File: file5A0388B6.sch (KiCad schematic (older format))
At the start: 40 parts, among them J1 test, J2 test, J3 test, J4 test, U1 AD7175-8, U2 ADR4520, U3 ADR445, Y1 16M

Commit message: 전해콘덴서 foot print 변경
전해 콘덴서 변경
Bypass 콘데서 OPAMP에 추가 하여야 함
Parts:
- C1, C10, C12, C18, C19, C2, C7: footprint Capacitors_SMD:C_1812_HandSoldering -> USER:C_1812_HandSoldering_Polar
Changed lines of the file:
@@
 F 0 "C2" H 3475 2350 50  0000 L CNN
 F 1 "10uF" H 3475 2150 50  0000 L CNN
-F 2 "Capacitors_SMD:C_1812_HandSoldering" H 3450 2250 50  0001 C CNN
+F 2 "USER:C_1812_HandSoldering_Polar" H 3450 2250 50  0001 C CNN
 F 3 "" H 3450 2250 50  0001 C CNN
 	1    3450 2250
@@
 F 0 "C1" H 3475 1400 50  0000 L CNN
 F 1 "10uF" H 3475 1200 50  0000 L CNN
-F 2 "Capacitors_SMD:C_1812_HandSoldering" H 3450 1300 50  0001 C CNN
+F 2 "USER:C_1812_HandSoldering_Polar" H 3450 1300 50  0001 C CNN
 F 3 "" H 3450 1300 50  0001 C CNN
 	1    3450 1300
@@
 F 0 "C12" H 6375 2250 50  0000 L CNN
 F 1 "10uF" H 6375 2050 50  0000 L CNN
-F 2 "Capacitors_SMD:C_1812_HandSoldering" H 6350 2150 50  0001 C CNN
+F 2 "USER:C_1812_HandSoldering_Polar" H 6350 2150 50  0001 C CNN
 F 3 "" H 6350 2150 50  0001 C CNN
 	1    6350 2150
@@
 F 0 "C10" H 5725 2500 50  0000 L CNN
 F 1 "10uF" H 5725 2300 50  0000 L CNN
-F 2 "Capacitors_SMD:C_1812_HandSoldering" H 5700 2400 50  0001 C CNN
+F 2 "USER:C_1812_HandSoldering_Polar" H 5700 2400 50  0001 C CNN
 F 3 "" H 5700 2400 50  0001 C CNN
 	1    5700 2400
@@
 F 0 "C7" H 5325 1400 50  0000 L CNN
 F 1 "10uF" H 5325 1200 50  0000 L CNN
-F 2 "Capacitors_SMD:C_1812_HandSoldering" H 5300 1300 50  0001 C CNN
+F 2 "USER:C_1812_HandSoldering_Polar" H 5300 1300 50  0001 C CNN
 F 3 "" H 5300 1300 50  0001 C CNN
 	1    5300 1300
@@
 F 0 "C19" H 9275 5300 50  0000 L CNN
 F 1 "10uF" H 9275 5100 50  0000 L CNN
-F 2 "Capacitors_SMD:C_1812_HandSoldering" H 9250 5200 50  0001 C CNN
+F 2 "USER:C_1812_HandSoldering_Polar" H 9250 5200 50  0001 C CNN
 F 3 "" H 9250 5200 50  0001 C CNN
 	1    9250 5200
@@
 F 0 "C18" H 9275 2900 50  0000 L CNN
 F 1 "10uF" H 9275 2700 50  0000 L CNN
-F 2 "Capacitors_SMD:C_1812_HandSoldering" H 9250 2800 50  0001 C CNN
+F 2 "USER:C_1812_HandSoldering_Polar" H 9250 2800 50  0001 C CNN
 F 3 "" H 9250 2800 50  0001 C CNN
 	1    9250 2800

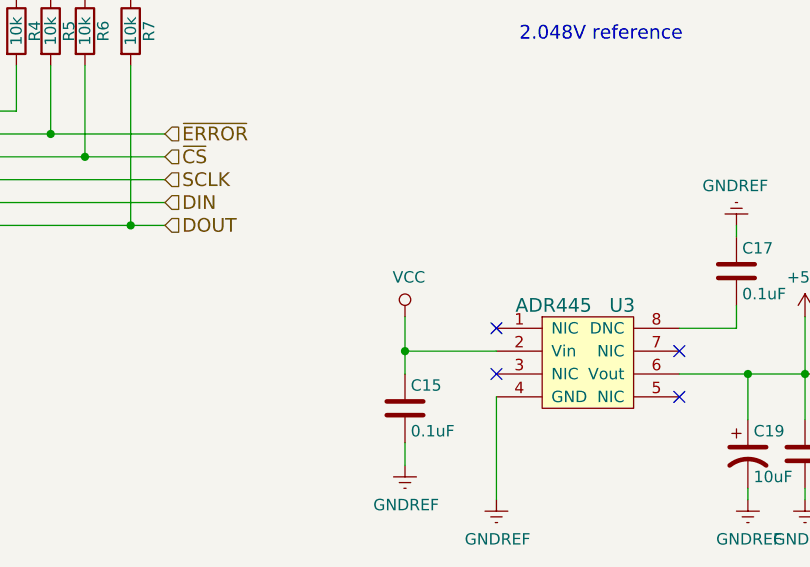
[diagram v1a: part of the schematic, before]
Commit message: 2차 PCB 1차 수정
1. ADR455 Vcc V12 수정
2. DCDC 입력전압 변경
3. Bypass 콘덴서 C66, C67 추가
4. SOIC 방향 표시
5. TLV431 PADS 변경
6. AQV258 Pin3 --> Pin2
7. 전해콘덴서 방향추가
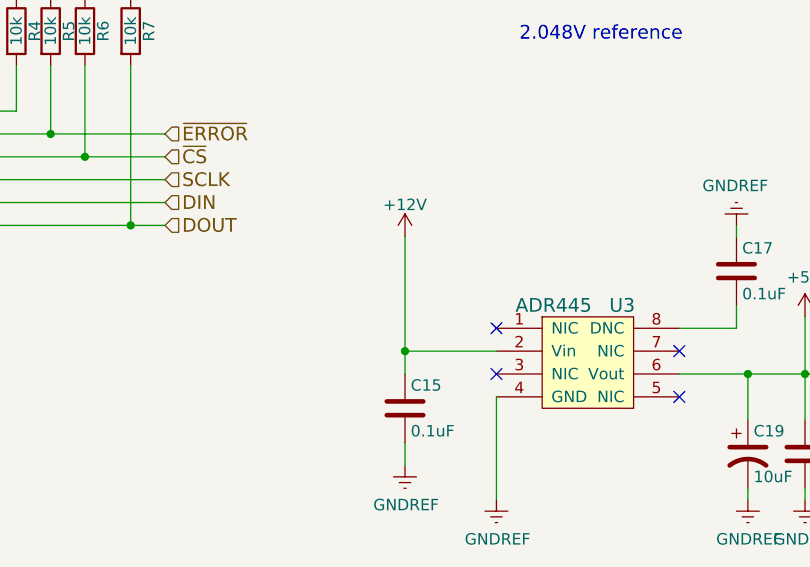
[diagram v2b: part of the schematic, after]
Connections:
- net VCC: no longer C15.1, U3.2 (Vin)
- new net +12V: C15.1, U3.2 (Vin)
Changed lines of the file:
@@
 $EndComp
 Wire Wire Line
-	7750 4600 7750 4850
+	7750 4250 7750 4850
 Wire Wire Line
 	7750 4750 8150 4750
@@
 Wire Wire Line
 	3150 4600 2950 4600
-$Comp
-L VCC #PWR031
-U 1 1 5AA57289
-P 7750 4600
-F 0 "#PWR031" H 7750 4450 50  0001 C CNN
-F 1 "VCC" H 7767 4773 50  0000 C CNN
-F 2 "" H 7750 4600 50  0001 C CNN
-F 3 "" H 7750 4600 50  0001 C CNN
-	1    7750 4600
-	1    0    0    -1
-$EndComp
 Text Notes 8250 5800 0    60   ~ 0
 5V reference\n
@@
 Connection ~ 3050 4400
 Connection ~ 3050 4600
+$Comp
+L +12V #PWR031
+U 1 1 5B1BD3CE
+P 7750 4250
+F 0 "#PWR031" H 7750 4100 50  0001 C CNN
+F 1 "+12V" H 7750 4390 50  0000 C CNN
+F 2 "" H 7750 4250 50  0001 C CNN
+F 3 "" H 7750 4250 50  0001 C CNN
+	1    7750 4250
+	1    0    0    -1
+$EndComp
 $EndSCHEMATC

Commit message: switch 수정
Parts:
- U2, U3: footprint Housings_SOIC:SOIC-8_3.9x4.9mm_Pitch1.27mm -> USER:SOIC-8_3.9x4.9mm_Pitch1.27mm
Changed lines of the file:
@@
 F 0 "U3" H 8700 4150 60  0000 C CNN
 F 1 "ADR445" H 8400 4150 60  0000 C CNN
-F 2 "Housings_SOIC:SOIC-8_3.9x4.9mm_Pitch1.27mm" H 8350 4350 60  0001 C CNN
+F 2 "USER:SOIC-8_3.9x4.9mm_Pitch1.27mm" H 8350 4350 60  0001 C CNN
 F 3 "" H 8350 4350 60  0001 C CNN
 	1    8350 4350
@@
 F 0 "U2" H 8700 1750 60  0000 C CNN
 F 1 "ADR4520" H 8400 1750 60  0000 C CNN
-F 2 "Housings_SOIC:SOIC-8_3.9x4.9mm_Pitch1.27mm" H 8350 1950 60  0001 C CNN
+F 2 "USER:SOIC-8_3.9x4.9mm_Pitch1.27mm" H 8350 1950 60  0001 C CNN
 F 3 "" H 8350 1950 60  0001 C CNN
 	1    8350 1950

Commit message: 2차PCB
U22 포함
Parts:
- D1, D2, D3: footprint LEDs:LED_0603_HandSoldering -> LEDs:LED_0805_HandSoldering
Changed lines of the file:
@@
 F 0 "D1" H 3700 5550 50  0000 C CNN
 F 1 "LED_ALT" H 3200 5550 50  0000 C CNN
-F 2 "LEDs:LED_0603_HandSoldering" H 3500 5600 50  0001 C CNN
+F 2 "LEDs:LED_0805_HandSoldering" H 3500 5600 50  0001 C CNN
 F 3 "~" H 3500 5600 50  0001 C CNN
 	1    3500 5600
@@
 F 0 "D2" H 3700 5700 50  0000 C CNN
 F 1 "LED_ALT" H 3200 5700 50  0000 C CNN
-F 2 "LEDs:LED_0603_HandSoldering" H 3500 5750 50  0001 C CNN
+F 2 "LEDs:LED_0805_HandSoldering" H 3500 5750 50  0001 C CNN
 F 3 "~" H 3500 5750 50  0001 C CNN
 	1    3500 5750
@@
 F 0 "D3" H 3700 5850 50  0000 C CNN
 F 1 "LED_ALT" H 3200 5850 50  0000 C CNN
-F 2 "LEDs:LED_0603_HandSoldering" H 3500 5900 50  0001 C CNN
+F 2 "LEDs:LED_0805_HandSoldering" H 3500 5900 50  0001 C CNN
 F 3 "~" H 3500 5900 50  0001 C CNN
 	1    3500 5900
